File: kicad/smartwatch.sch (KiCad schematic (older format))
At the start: 17 parts, among them X1 32MHz, X2 32.768kHz

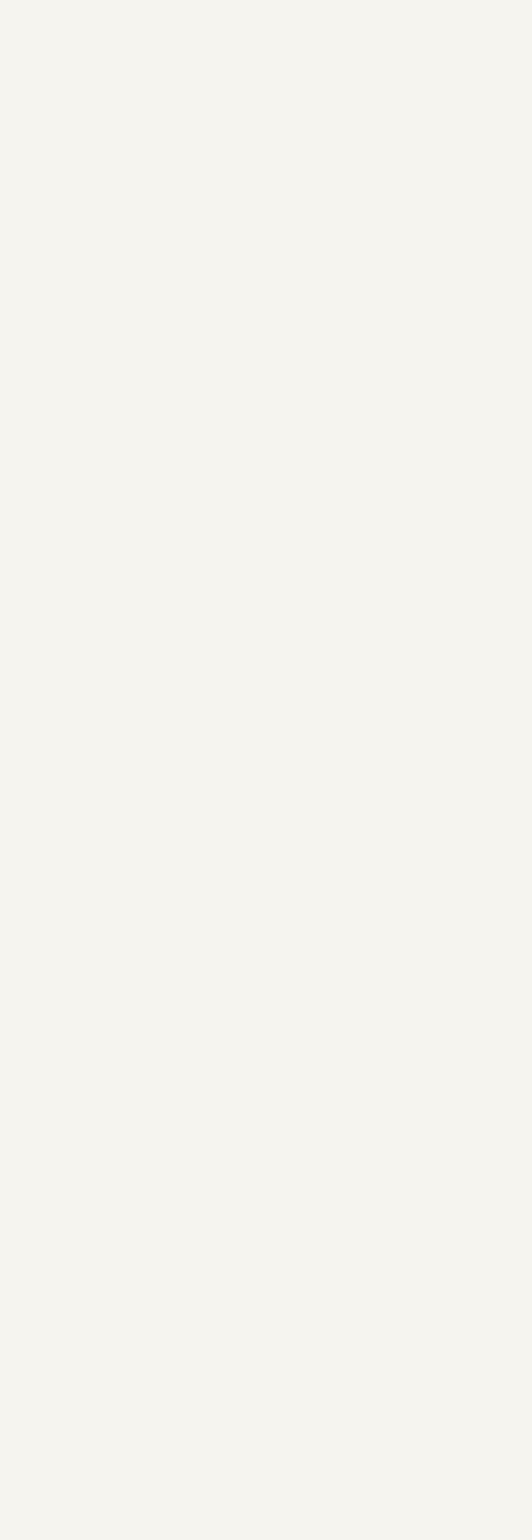
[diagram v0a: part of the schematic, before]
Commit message: Drew most schema components. Touch sensor still remaining.
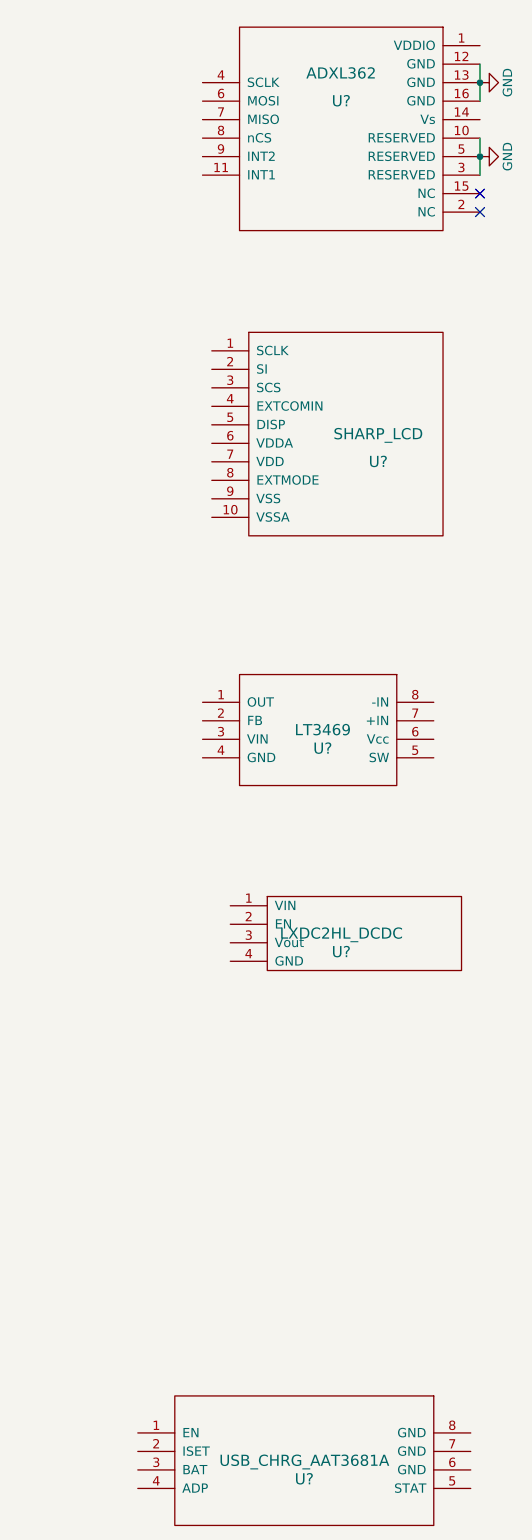
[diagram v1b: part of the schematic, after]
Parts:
- added U?: ADXL362, symbol ADXL362
- added U?: SHARP_LCD, symbol SHARP_LCD
- added U?: LT3469, symbol LT3469
- added U?: LXDC2HL_DCDC, symbol LXDC2HL_DCDC
- added U?: USB_CHRG_AAT3681A, symbol USB_CHRG_AAT3681A
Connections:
- net GND: now also U?.10 (RESERVED), U?.12 (GND), U?.13 (GND), U?.16 (GND), U?.3 (RESERVED), U?.5 (RESERVED)
- no-connect marks 1 -> 3
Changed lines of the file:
@@
 LIBS:valves
 LIBS:nrf52832
+LIBS:adxl362
+LIBS:sharp_lcd
+LIBS:lt3469
+LIBS:lxdc2hl_dcdc
+LIBS:usb_chrg_aat3681a
+LIBS:smartwatch-cache
 EELAYER 25 0
 EELAYER END
-$Descr A4 11693 8268
+$Descr A3 16535 11693
 encoding utf-8
 Sheet 1 1
@@
 Wire Wire Line
 	4250 1600 4250 1900
+$Comp
+L ADXL362 U?
+U 1 1 58A0D490
+P 14350 1500
+F 0 "U?" H 14350 1650 60  0000 C CNN
+F 1 "ADXL362" H 14350 1800 60  0000 C CNN
+F 2 "" H 14250 1500 60  0001 C CNN
+F 3 "" H 14250 1500 60  0001 C CNN
+	1    14350 1500
+	1    0    0    -1
+$EndComp
+Wire Wire Line
+	15100 1150 15100 1350
+Connection ~ 15100 1250
+$Comp
+L GND #PWR?
+U 1 1 58A0D7D5
+P 15100 1250
+F 0 "#PWR?" H 15100 1000 50  0001 C CNN
+F 1 "GND" H 15100 1100 50  0000 C CNN
+F 2 "" H 15100 1250 50  0000 C CNN
+F 3 "" H 15100 1250 50  0000 C CNN
+	1    15100 1250
+	0    -1   -1   0
+$EndComp
+Wire Wire Line
+	15100 1550 15100 1750
+Connection ~ 15100 1650
+$Comp
+L GND #PWR?
+U 1 1 58A0D8AD
+P 15100 1650
+F 0 "#PWR?" H 15100 1400 50  0001 C CNN
+F 1 "GND" H 15100 1500 50  0000 C CNN
+F 2 "" H 15100 1650 50  0000 C CNN
+F 3 "" H 15100 1650 50  0000 C CNN
+	1    15100 1650
+	0    -1   -1   0
+$EndComp
+NoConn ~ 15100 1850
+NoConn ~ 15100 1950
+$Comp
+L SHARP_LCD U?
+U 1 1 58A0DD6F
+P 14350 3150
+F 0 "U?" H 14550 3000 60  0000 C CNN
+F 1 "SHARP_LCD" H 14550 3150 60  0000 C CNN
+F 2 "" H 14350 3150 60  0001 C CNN
+F 3 "" H 14350 3150 60  0001 C CNN
+	1    14350 3150
+	1    0    0    -1
+$EndComp
+$Comp
+L LT3469 U?
+U 1 1 58A0DF9B
+P 14250 4750
+F 0 "U?" H 14250 4650 60  0000 C CNN
+F 1 "LT3469" H 14250 4750 60  0000 C CNN
+F 2 "" H 14250 4750 60  0001 C CNN
+F 3 "" H 14250 4750 60  0001 C CNN
+	1    14250 4750
+	1    0    0    -1
+$EndComp
+$Comp
+L LXDC2HL_DCDC U?
+U 1 1 58A0E0F7
+P 14350 5850
+F 0 "U?" H 14350 5750 60  0000 C CNN
+F 1 "LXDC2HL_DCDC" H 14350 5850 60  0000 C CNN
+F 2 "" H 14350 5850 60  0001 C CNN
+F 3 "" H 14350 5850 60  0001 C CNN
+	1    14350 5850
+	1    0    0    -1
+$EndComp
+$Comp
+L USB_CHRG_AAT3681A U?
+U 1 1 58A0E414
+P 14150 8700
+F 0 "U?" H 14150 8600 60  0000 C CNN
+F 1 "USB_CHRG_AAT3681A" H 14150 8700 60  0000 C CNN
+F 2 "" H 14150 8700 60  0001 C CNN
+F 3 "" H 14150 8700 60  0001 C CNN
+	1    14150 8700
+	1    0    0    -1
+$EndComp
 $EndSCHEMATC

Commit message: piirtelyä ja speksi luettu
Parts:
- added P?: sw1, symbol CONN_01X02
- added P?: sw2, symbol CONN_01X02
- added P?: sw3, symbol CONN_01X02
- added P?: sw4, symbol CONN_01X02
- added U?: swd_port, symbol swd_port
- added U?: KXG03, symbol KXG03
- added U?: KMX62, symbol KMX62
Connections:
- net GND: now also P?.2 (P2), P?.2 (P2), P?.2 (P2), P?.2 (P2), U?.4 (GND)
- net VDD: now also U?.1 (VREF)
- net SWDCLK: now reaches U?.25 (SWDCLK)
- net SWDCLK: now also U?.3 (SWDCLK)
- net SWDIO: now reaches U?.26 (SWDIO)
- net SWDIO: now also U?.2 (SWDIO)
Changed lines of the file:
@@
 LIBS:lxdc2hl_dcdc
 LIBS:usb_chrg_aat3681a
+LIBS:swd_port
+LIBS:kxg03
+LIBS:kmx62
 LIBS:smartwatch-cache
 EELAYER 25 0
@@
 	1    0    0    -1
 $EndComp
+$Comp
+L swd_port U?
+U 1 1 58A1D8A3
+P 8500 4450
+F 0 "U?" H 8500 4350 60  0000 C CNN
+F 1 "swd_port" H 8500 4450 60  0000 C CNN
+F 2 "" H 8500 4450 60  0001 C CNN
+F 3 "" H 8500 4450 60  0001 C CNN
+	1    8500 4450
+	1    0    0    -1
+$EndComp
+Text GLabel 6650 4300 2    60   Input ~ 0
+SWDCLK
+Text GLabel 6650 4150 2    60   Input ~ 0
+SWDIO
+Text GLabel 7650 4400 0    60   Input ~ 0
+SWDIO
+Text GLabel 7650 4500 0    60   Input ~ 0
+SWDCLK
+$Comp
+L GND #PWR?
+U 1 1 58A1DA06
+P 7650 4600
+F 0 "#PWR?" H 7650 4350 50  0001 C CNN
+F 1 "GND" H 7650 4450 50  0000 C CNN
+F 2 "" H 7650 4600 50  0000 C CNN
+F 3 "" H 7650 4600 50  0000 C CNN
+	1    7650 4600
+	1    0    0    -1
+$EndComp
+$Comp
+L VDD #PWR?
+U 1 1 58A1DC87
+P 7650 4300
+F 0 "#PWR?" H 7650 4150 50  0001 C CNN
+F 1 "VDD" H 7650 4450 50  0000 C CNN
+F 2 "" H 7650 4300 50  0000 C CNN
+F 3 "" H 7650 4300 50  0000 C CNN
+	1    7650 4300
+	1    0    0    -1
+$EndComp
+$Comp
+L KXG03 U?
+U 1 1 58A743BA
+P 11550 8700
+F 0 "U?" H 11550 8600 60  0000 C CNN
+F 1 "KXG03" H 11550 8700 60  0000 C CNN
+F 2 "" H 11550 8700 60  0001 C CNN
+F 3 "" H 11550 8700 60  0001 C CNN
+	1    11550 8700
+	1    0    0    -1
+$EndComp
+$Comp
+L KMX62 U?
+U 1 1 58A747F2
+P 8900 8750
+F 0 "U?" H 8900 8650 60  0000 C CNN
+F 1 "KMX62" H 8900 8750 60  0000 C CNN
+F 2 "" H 8900 8750 60  0001 C CNN
+F 3 "" H 8900 8750 60  0001 C CNN
+	1    8900 8750
+	1    0    0    -1
+$EndComp
+$Comp
+L CONN_01X02 P?
+U 1 1 58A74AE2
+P 3450 7350
+F 0 "P?" H 3450 7500 50  0000 C CNN
+F 1 "sw1" V 3550 7350 50  0000 C CNN
+F 2 "" H 3450 7350 50  0000 C CNN
+F 3 "" H 3450 7350 50  0000 C CNN
+	1    3450 7350
+	1    0    0    -1
+$EndComp
+$Comp
+L CONN_01X02 P?
+U 1 1 58A74BA1
+P 3450 7750
+F 0 "P?" H 3450 7900 50  0000 C CNN
+F 1 "sw2" V 3550 7750 50  0000 C CNN
+F 2 "" H 3450 7750 50  0000 C CNN
+F 3 "" H 3450 7750 50  0000 C CNN
+	1    3450 7750
+	1    0    0    -1
+$EndComp
+$Comp
+L CONN_01X02 P?
+U 1 1 58A74DAE
+P 3450 8100
+F 0 "P?" H 3450 8250 50  0000 C CNN
+F 1 "sw3" V 3550 8100 50  0000 C CNN
+F 2 "" H 3450 8100 50  0000 C CNN
+F 3 "" H 3450 8100 50  0000 C CNN
+	1    3450 8100
+	1    0    0    -1
+$EndComp
+$Comp
+L CONN_01X02 P?
+U 1 1 58A74DFD
+P 3450 8450
+F 0 "P?" H 3450 8600 50  0000 C CNN
+F 1 "sw4" V 3550 8450 50  0000 C CNN
+F 2 "" H 3450 8450 50  0000 C CNN
+F 3 "" H 3450 8450 50  0000 C CNN
+	1    3450 8450
+	1    0    0    -1
+$EndComp
+$Comp
+L GND #PWR?
+U 1 1 58A74FF8
+P 3250 7400
+F 0 "#PWR?" H 3250 7150 50  0001 C CNN
+F 1 "GND" H 3250 7250 50  0000 C CNN
+F 2 "" H 3250 7400 50  0000 C CNN
+F 3 "" H 3250 7400 50  0000 C CNN
+	1    3250 7400
+	1    0    0    -1
+$EndComp
+$Comp
+L GND #PWR?
+U 1 1 58A75087
+P 3250 7800
+F 0 "#PWR?" H 3250 7550 50  0001 C CNN
+F 1 "GND" H 3250 7650 50  0000 C CNN
+F 2 "" H 3250 7800 50  0000 C CNN
+F 3 "" H 3250 7800 50  0000 C CNN
+	1    3250 7800
+	1    0    0    -1
+$EndComp
+$Comp
+L GND #PWR?
+U 1 1 58A750D5
+P 3250 8150
+F 0 "#PWR?" H 3250 7900 50  0001 C CNN
+F 1 "GND" H 3250 8000 50  0000 C CNN
+F 2 "" H 3250 8150 50  0000 C CNN
+F 3 "" H 3250 8150 50  0000 C CNN
+	1    3250 8150
+	1    0    0    -1
+$EndComp
+$Comp
+L GND #PWR?
+U 1 1 58A75123
+P 3250 8500
+F 0 "#PWR?" H 3250 8250 50  0001 C CNN
+F 1 "GND" H 3250 8350 50  0000 C CNN
+F 2 "" H 3250 8500 50  0000 C CNN
+F 3 "" H 3250 8500 50  0000 C CNN
+	1    3250 8500
+	1    0    0    -1
+$EndComp

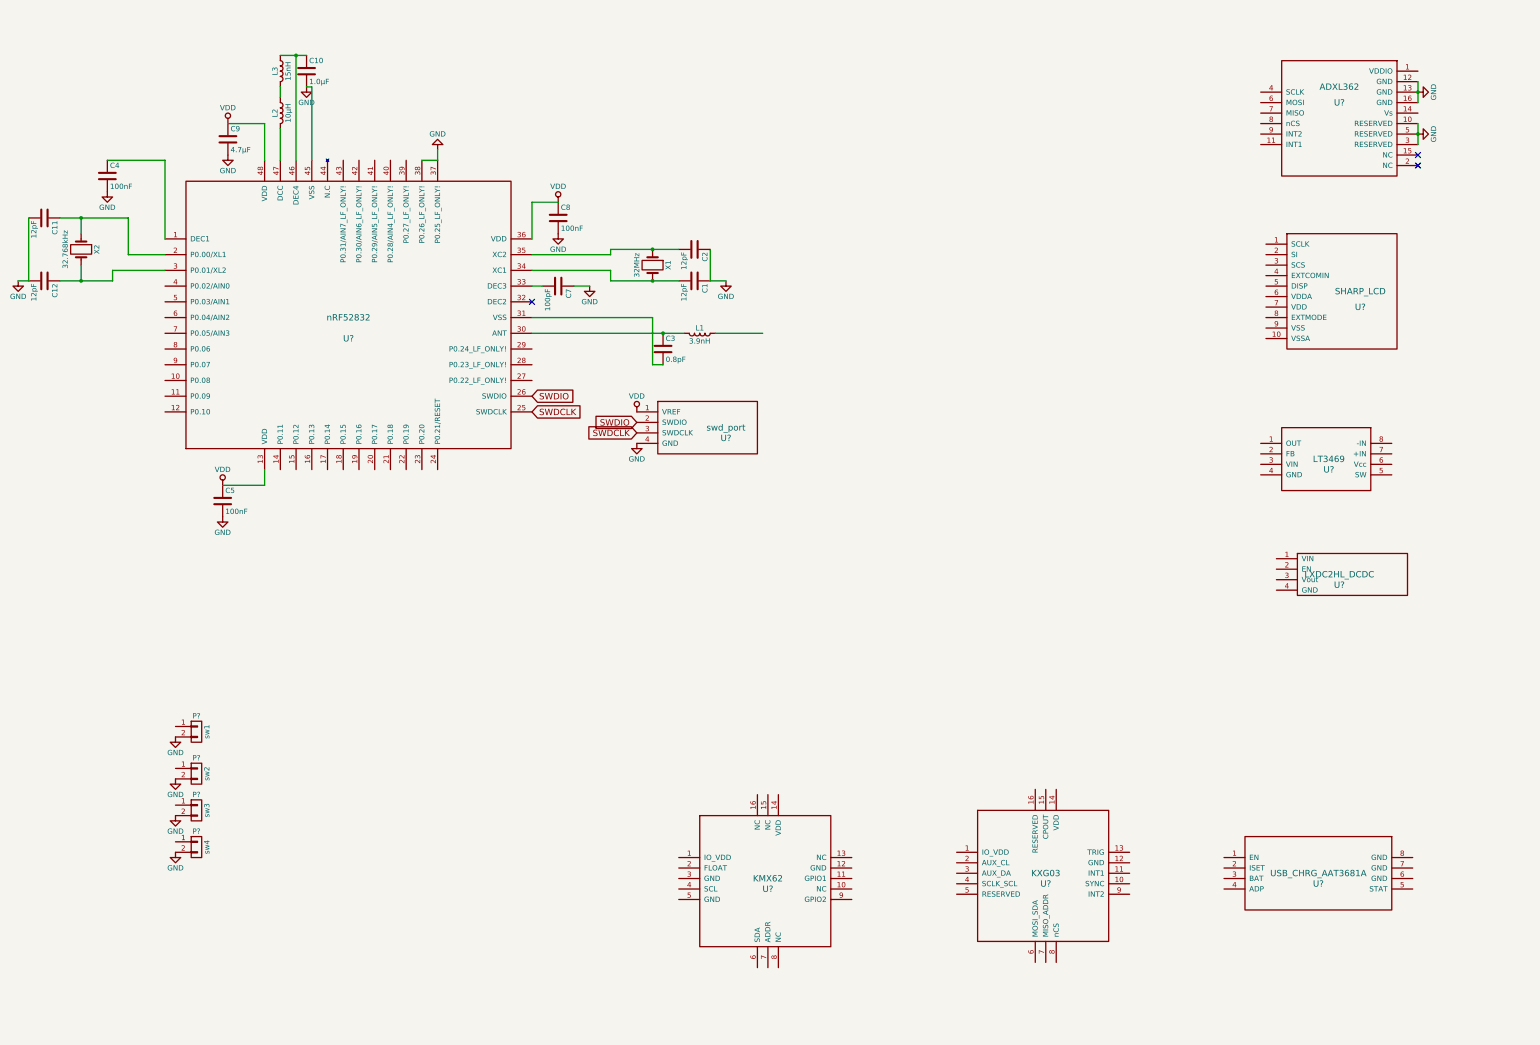
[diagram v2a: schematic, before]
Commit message: Skemassa melkein kaikki vedot vedetty. Pitää vielä tarkistus kierros
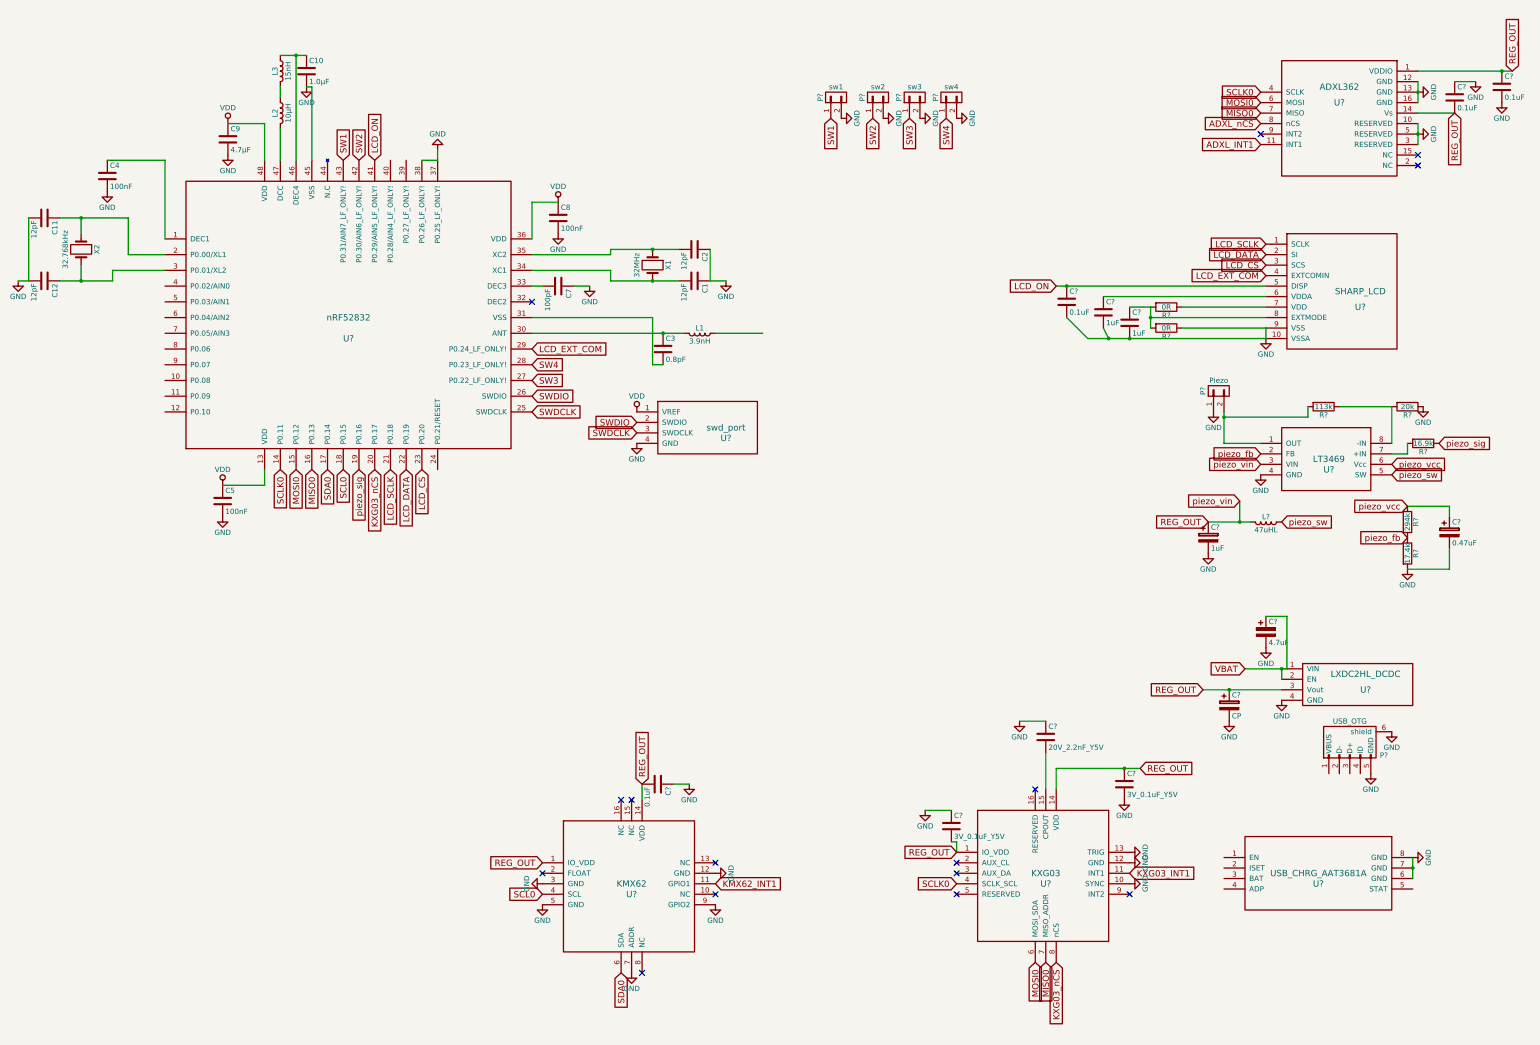
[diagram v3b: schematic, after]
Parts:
- added C?: 20V_2.2nF_Y5V, symbol C
- added C? (x2): 3V_0.1uF_Y5V, symbol C
- added C?: 4.7uF, symbol CP
- added C?: CP, symbol CP
- added C?: 0.47uF, symbol CP
- added C?: 1uF, symbol CP
- added C? (x4): 0.1uF, symbol C
- added C? (x2): 1uF, symbol C
- added L?: 47uHL, symbol L
- added P?: USB_OTG, symbol USB_OTG
- added P?: Piezo, symbol CONN_01X02
- added R?: 113k, symbol R
- added R?: 20k, symbol R
- added R?: 294k, symbol R
- added R?: 17.4k, symbol R
- added R?: 16.9k, symbol R
- added R? (x2): 0R, symbol R
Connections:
- net GND: now also U?.10 (SYNC), U?.10 (VSSA), U?.12 (GND), U?.12 (GND), U?.13 (TRIG), U?.3 (GND), U?.4 (GND), U?.4 (GND), U?.5 (GND), U?.6 (GND), U?.7 (ADDR), U?.7 (GND), U?.8 (GND), U?.9 (GPIO2), U?.9 (VSS), C?.1, C?.1, C?.1, C?.1, C?.2, C?.2, C?.2, C?.2, C?.2, C?.2, C?.2, C?.2, C?.2, P?.1 (P1), P?.5 (GND), P?.6 (shield), R?.1, R?.1, R?.2
- net SCLK0: now reaches U?.14 (P0.11)
- net SCLK0: now also U?.4 (SCLK), U?.4 (SCLK_SCL)
- net MOSI0: now reaches U?.15 (P0.12)
- net MOSI0: now also U?.6 (MOSI), U?.6 (MOSI_SDA)
- net MISO0: now reaches U?.16 (P0.13)
- net MISO0: now also U?.7 (MISO), U?.7 (MISO_ADDR)
- net SDA0: now reaches U?.17 (P0.14)
- net SDA0: now also U?.6 (SDA)
- net SCL0: now reaches U?.18 (P0.15)
- net SCL0: now also U?.4 (SCL)
- net piezo_sig: now reaches U?.19 (P0.16)
- net piezo_sig: now also R?.1
- net KXG03_nCS: now reaches U?.20 (P0.17)
- net KXG03_nCS: now also U?.8 (nCS)
- net LCD_SCLK: now reaches U?.21 (P0.18)
- net LCD_SCLK: now also U?.1 (SCLK)
- net LCD_DATA: now reaches U?.22 (P0.19)
- net LCD_DATA: now also U?.2 (SI)
- net LCD_CS: now reaches U?.23 (P0.20)
- net LCD_CS: now also U?.3 (SCS)
- net SW3: now reaches U?.27 (P0.22_LF_ONLY!)
- net SW3: now also P?.1 (P1)
- net SW4: now reaches U?.28 (P0.23_LF_ONLY!)
- net SW4: now also P?.1 (P1)
- net LCD_EXT_COM: now reaches U?.29 (P0.24_LF_ONLY!)
- net LCD_EXT_COM: now also U?.4 (EXTCOMIN)
- net LCD_ON: now reaches U?.41 (P0.29/AIN5_LF_ONLY!)
- net LCD_ON: now also U?.5 (DISP), C?.1
- net SW2: now reaches U?.42 (P0.30/AIN6_LF_ONLY!)
- net SW2: now also P?.1 (P1)
- net SW1: now reaches U?.43 (P0.31/AIN7_LF_ONLY!)
- net SW1: now also P?.1 (P1)
- net REG_OUT: now reaches U?.1 (VDDIO)
- net REG_OUT: now also U?.1 (IO_VDD), U?.1 (IO_VDD), U?.14 (VDD), U?.14 (VDD), U?.14 (Vs), U?.3 (VIN), U?.3 (Vout), C?.1, C?.1, C?.1, C?.1, C?.2, C?.2, C?.2, L?.2
- net ADXL_INT1: now reaches U?.11 (INT1)
- net ADXL_nCS: now reaches U?.8 (nCS)
- net at U?.6 (VDDA): now also C?.1
- net at U?.7 (VDD): now also R?.1
- net at U?.8 (EXTMODE): now also C?.1, R?.2, R?.2
- net at U?.1 (OUT): now also P?.2 (P2), R?.2
- net piezo_fb: now reaches U?.2 (FB)
- net piezo_fb: now also R?.1, R?.2
- net piezo_sw: now reaches U?.5 (SW)
- net piezo_sw: now also L?.1
- net piezo_vcc: now reaches U?.6 (Vcc)
- net piezo_vcc: now also C?.1, R?.1
- net at U?.7 (+IN): now also R?.2
- net at U?.8 (-IN): now also R?.1, R?.2
- net VBAT: now reaches U?.1 (VIN)
- net VBAT: now also U?.2 (EN), C?.1
- net KXG03_INT1: now reaches U?.11 (INT1)
- net at U?.15 (CPOUT): now also C?.2
- net KMX62_INT1: now reaches U?.11 (GPIO1)
- no-connect marks 3 -> 15
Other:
- moved on the sheet: P?, U?

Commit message: lisäsin datasheetit_yms
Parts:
- added D?: LED, symbol LED
- added P?: BAT1+, symbol CONN_01X02
- added R?: 1.75k, symbol R
- added R?: 16k=100mA, symbol R
- gave numbers to parts that had none: 36
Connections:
- net VDD is gone; now on net REG_OUT: C5.1, C8.1, C9.1, U1.13 (VDD), U1.36 (VDD), U1.48 (VDD), U3.1 (VREF)
- net GND: now also P?.2 (P2), R?.2
- net KXG03_INT1: now also U1.12 (P0.10)
- net REG_OUT: now also C16.1, U8.6 (VDDA)
- net USB_V: now reaches U5.1 (EN)
- net USB_V: now also P6.1 (VBUS), U5.4 (ADP), D?.2 (A)
- net at U5.2 (ISET): now also R?.1
- net BAT_V: now reaches U5.3 (BAT)
- net BAT_V: now also P?.1 (P1)
- net at U5.5 (STAT): now also R?.1
- new net: D?.1 (K), R?.2
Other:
- moved on the sheet: C14, U5
